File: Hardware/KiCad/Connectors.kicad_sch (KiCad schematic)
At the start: 49 parts

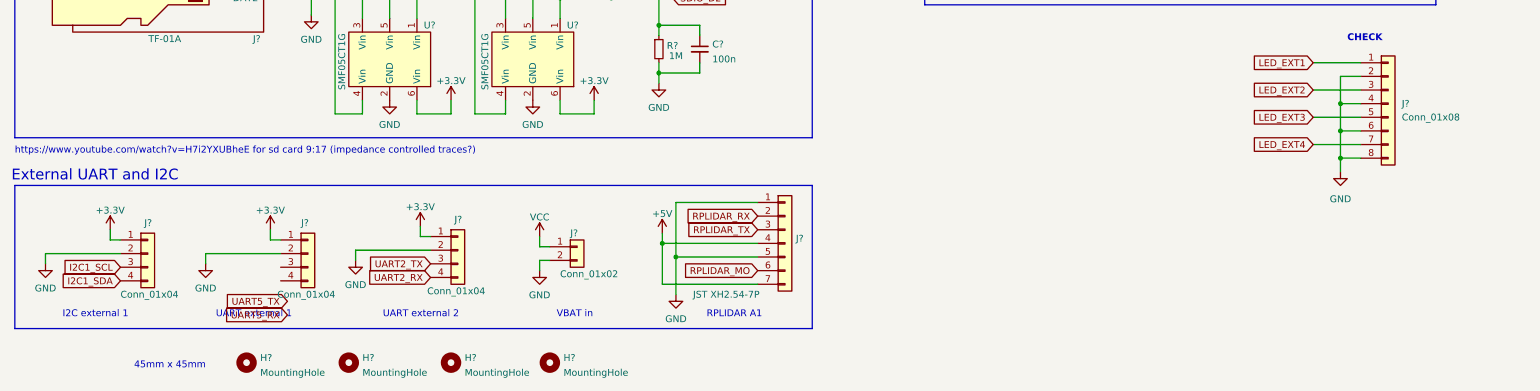
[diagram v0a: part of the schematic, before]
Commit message: Added more footprints
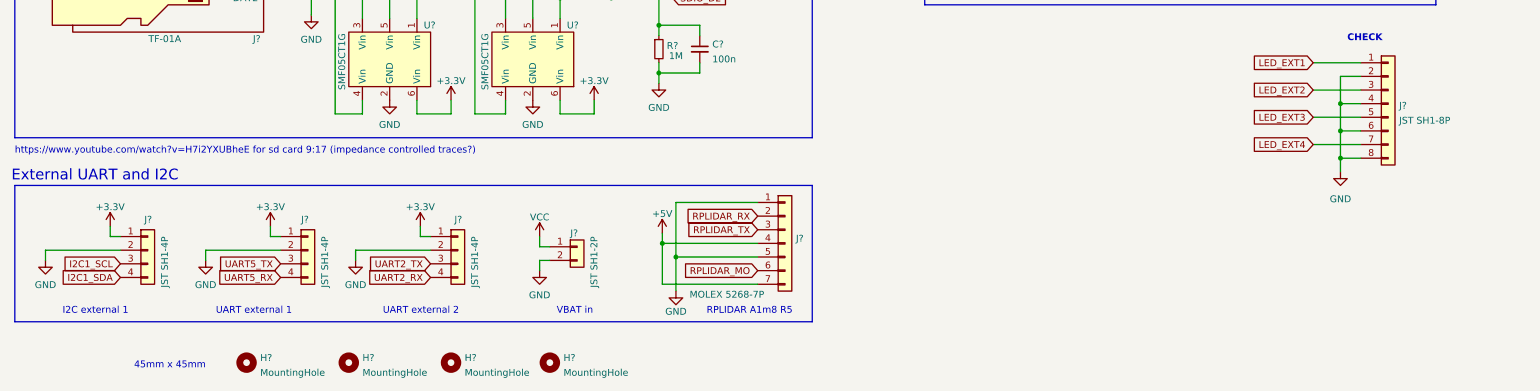
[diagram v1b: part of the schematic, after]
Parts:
- C? (x7): footprint (none) -> Capacitor_SMD:C_0402_1005Metric
- FB? (x3): footprint (none) -> Inductor_SMD:L_0603_1608Metric
- H? (x4): footprint (none) -> MountingHole:MountingHole_3.2mm_M3_ISO14580_Pad
- J? (x3): value Conn_01x04 -> JST SH1-4P; footprint (none) -> Connector_JST:JST_SH_SM04B-SRSS-TB_1x04-1MP_P1.00mm_Horizontal
- J?: value Conn_01x08 -> JST SH1-8P; footprint (none) -> Connector_JST:JST_SH_SM08B-SRSS-TB_1x08-1MP_P1.00mm_Horizontal
- J?: value Conn_01x02 -> JST SH1-2P; footprint (none) -> Connector_JST:JST_SHL_SM02B-SHLS-TF_1x02-1MP_P1.00mm_Horizontal
- J?: footprint (none) -> Connector_PinHeader_1.00mm:PinHeader_2x05_P1.00mm_Vertical_SMD
- J?: value JST XH2.54-7P -> MOLEX 5268-7P; footprint (none) -> Connector_Molex:Molex_SPOX_5268-07A_1x07_P2.50mm_Horizontal
- J?: footprint (none) -> Connector_PinHeader_2.54mm:PinHeader_2x08_P2.54mm_Horizontal
- J?: footprint (none) -> Connector_PinHeader_2.54mm:PinHeader_1x08_P2.54mm_Vertical
- R? (x13): footprint (none) -> Resistor_SMD:R_0402_1005Metric
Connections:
- net UART5_RX: now also J?.4 (Pin_4)
- net UART5_TX: now also J?.3 (Pin_3)
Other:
- note added: "RPLIDAR A1m8 R5"
- note removed: "RPLIDAR A1"
- moved on the sheet: J?

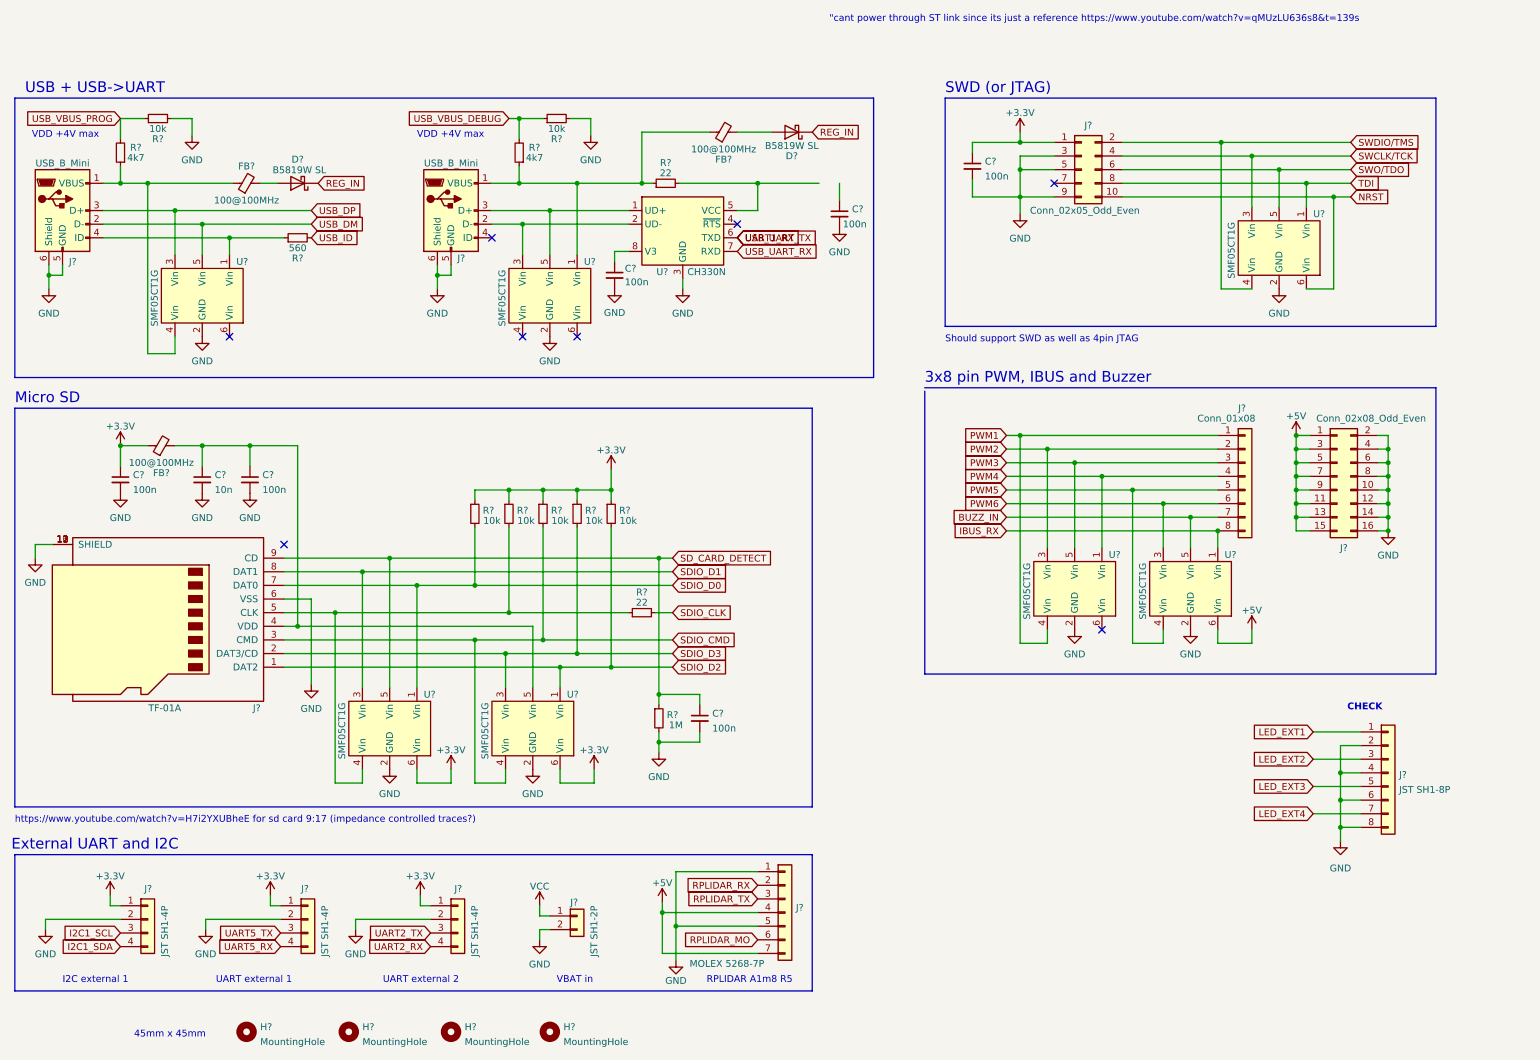
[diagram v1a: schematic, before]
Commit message: added all footprints and reorganized schematic
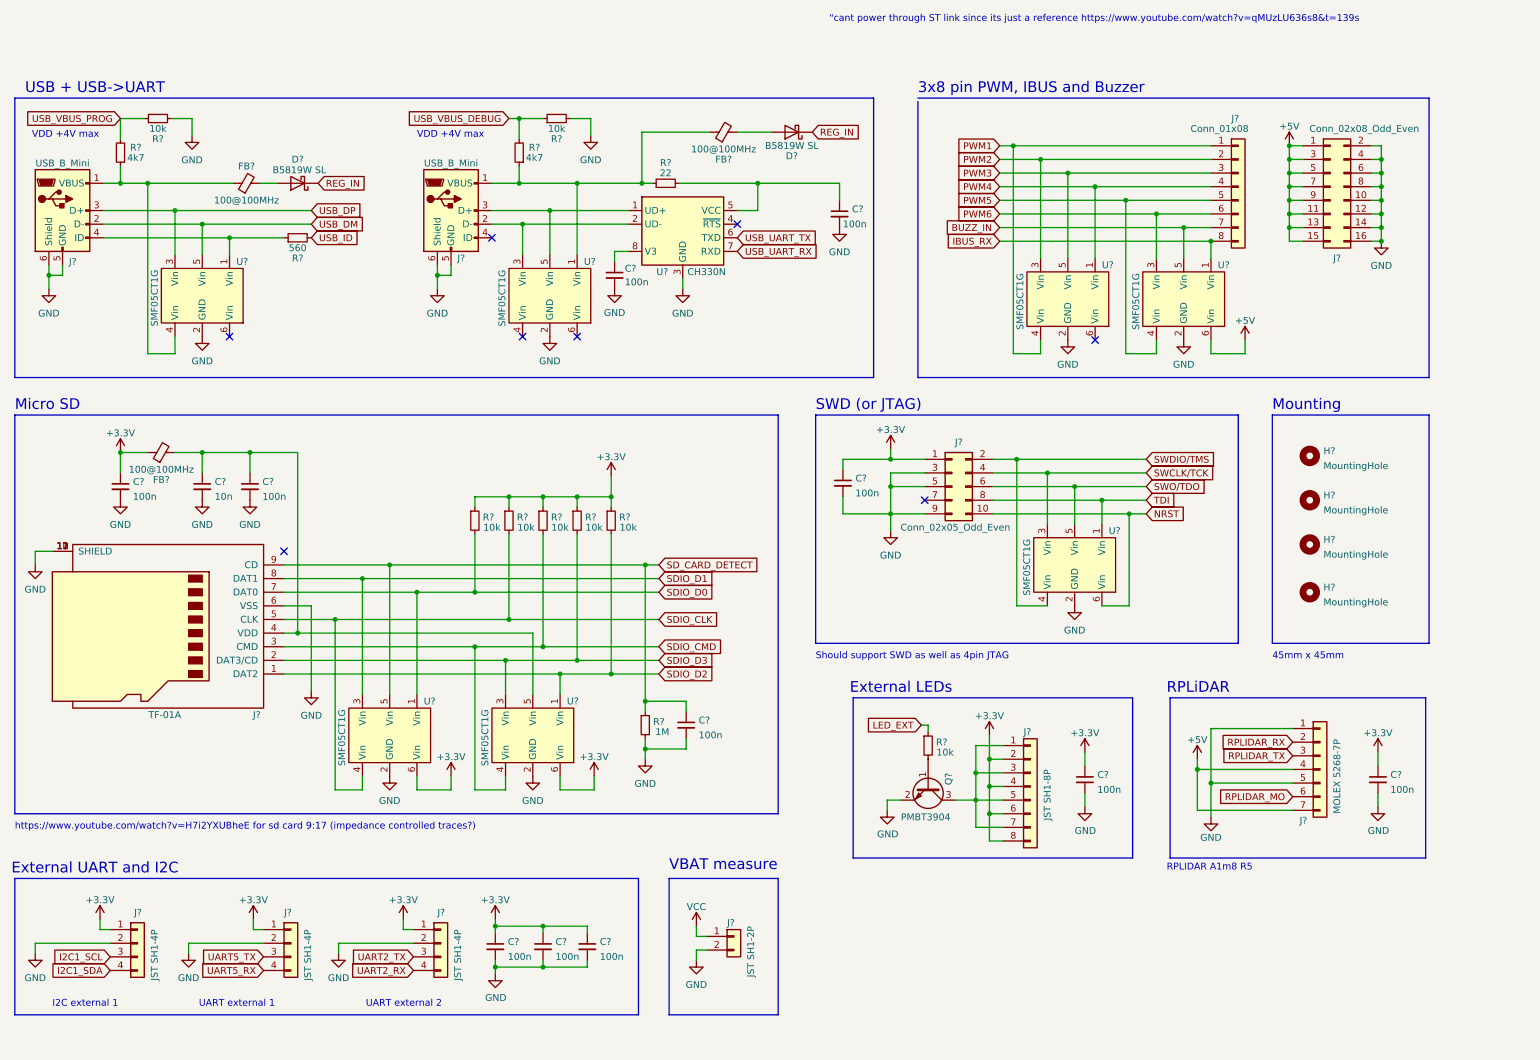
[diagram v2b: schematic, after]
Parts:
- removed R?: 22, Resistor_SMD:R_0402_1005Metric, symbol Device:R_Small
- added C? (x5): 100n, Capacitor_SMD:C_0402_1005Metric, symbol Device:C_Small
- added Q?: PMBT3904, Package_TO_SOT_SMD:SOT-23, symbol Device:Q_NPN_BEC
- added R?: 10k, Resistor_SMD:R_0402_1005Metric, symbol Device:R_Small
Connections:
- net LED_EXT2 is gone; now on an unnamed net: J?.3 (Pin_3)
- net LED_EXT3 is gone; now on an unnamed net: J?.5 (Pin_5)
- net LED_EXT4 is gone; now on an unnamed net: J?.7 (Pin_7)
- net +3V3: now also J?.2 (Pin_2), J?.4 (Pin_4), J?.6 (Pin_6), J?.8 (Pin_8), C?.1, C?.1, C?.1, C?.1, C?.1
- net GND: now also C?.2, C?.2, C?.2, C?.2, C?.2, Q?.2 (E); no longer J?.2 (Pin_2), J?.4 (Pin_4), J?.6 (Pin_6), J?.8 (Pin_8)
- net SDIO_CLK: now also J?.5 (CLK), R?.2, U?.4 (Vin)
- net at R?.2, U?.5 (VCC): now also C?.1
- net LED_EXT1: no longer names the net of J?.1 (Pin_1)
- net LED_EXT1: now also Q?.3 (C)
- net UART1_RX renamed USB_UART_TX
- new net: Q?.1 (B), R?.2
- new net LED_EXT: R?.1
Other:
- note added: "External LEDs"
- note added: "Mounting"
- note added: "RPLiDAR"
- note added: "VBAT measure"
- note removed: "CHECK"
- note removed: "VBAT in"
- moved on the sheet: C?, FB?, H?, J?, R?, U?
